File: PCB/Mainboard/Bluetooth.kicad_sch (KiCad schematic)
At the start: 22 parts, among them J10 U.FL, J11 JST-PH 01x02, U10 BTM331

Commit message: Update schematic and lay-out
- Swap out CP2102N, ATmega328PB and CP with new Kicad 6 symbol
- Correct all links to point to new zoudio_symbols and zoudio_footprint libraries
- Lay-out updated, only antenna is left to update.
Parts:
- AE1: footprint ZOUDIO-footprints:Texas_SWRA117D_2.4GHz_Left -> zoudio_footprints:Texas_SWRA117D_2.4GHz_Left
- U10: footprint ZOUDIO-footprints:BTM331 -> zoudio_footprints:BTM331; symbol ZOUDIO-symbols:BTM331 -> zoudio_symbols:BTM331
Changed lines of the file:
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@@
     (pin "2")
   )
-  (symbol (lib_id "ZOUDIO-symbols:BTM331") (at 114.3 101.6 0) (unit 1)
+  (symbol (lib_id "zoudio_symbols:BTM331") (at 114.3 101.6 0) (unit 1)
     (in_bom yes) (on_board yes)
     (property "Reference" "U10" (id 0) (at 114.3 100.33 0))
     (property "Value" "BTM331" (id 1) (at 114.3 102.87 0))
-    (property "Footprint" "ZOUDIO-footprints:BTM331" (id 2) (at 102.87 93.98 0)
+    (property "Footprint" "zoudio_footprints:BTM331" (id 2) (at 102.87 93.98 0)
       (effects (font (size 1.27 1.27)) hide)
     )
@@
       (effects (font (size 1.27 1.27)) (justify right))
     )
-    (property "Footprint" "ZOUDIO-footprints:Texas_SWRA117D_2.4GHz_Left" (id 2) (at 123.19 52.07 0)
-      (effects (font (size 1.27 1.27)) hide)
-    )
+    (property "Footprint" "zoudio_footprints:Texas_SWRA117D_2.4GHz_Left" (id 2) (at 123.19 52.07 0)
+      (effects (font (size 1.27 1.27)) hide)
+    )

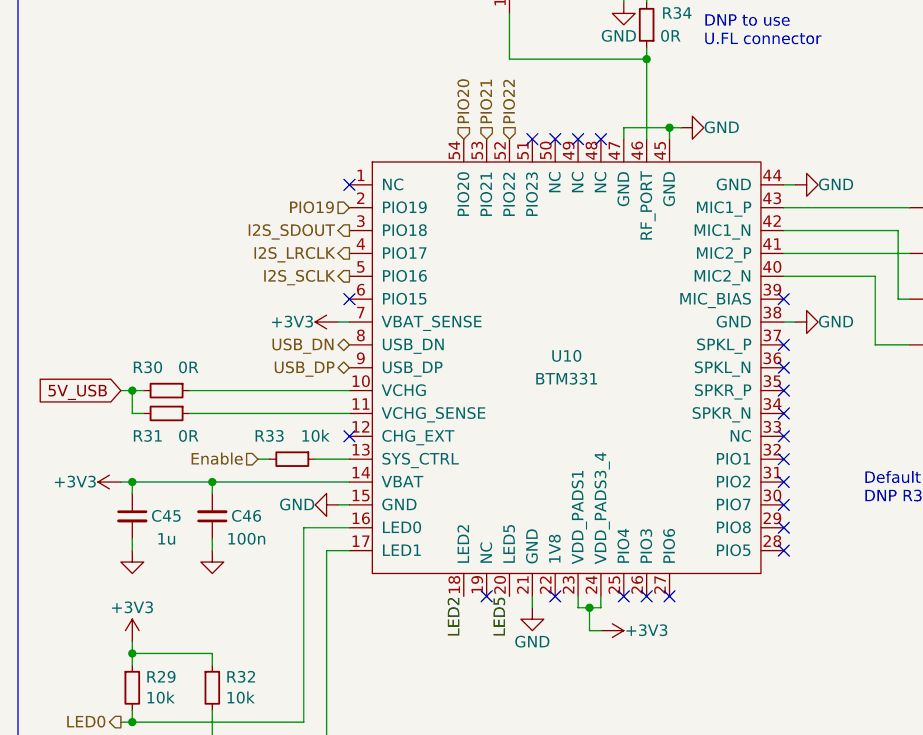
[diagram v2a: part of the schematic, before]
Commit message: Mainboard: version 1.1.1
- No change in electrical connectivity
- Make 3D model more complete
- Improvements in paste layer for manufacturability
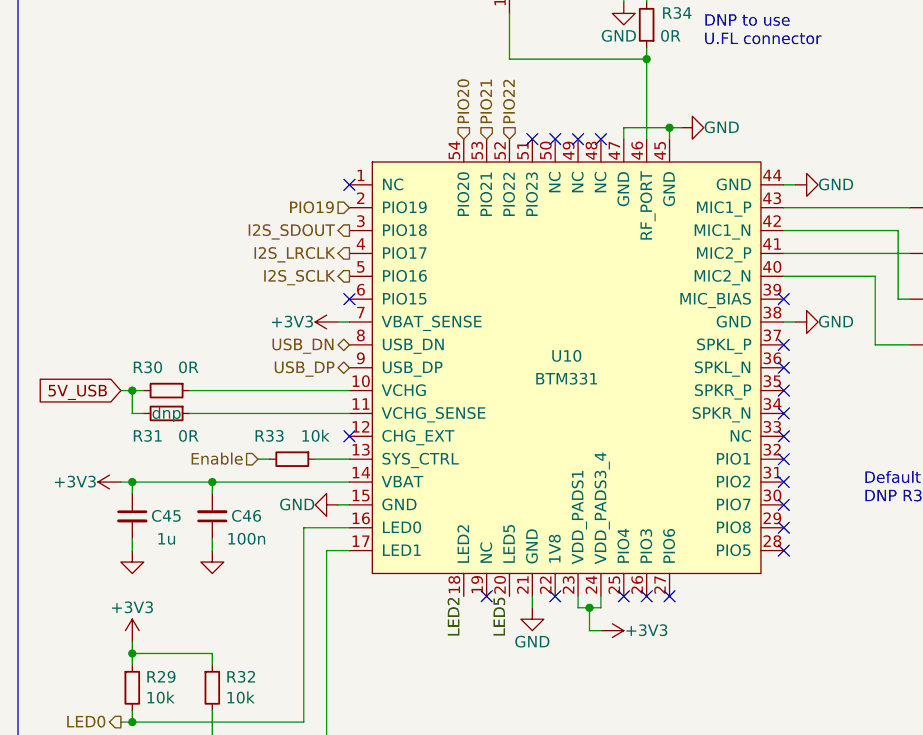
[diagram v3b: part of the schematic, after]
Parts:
- R31: Config (none) -> dnp
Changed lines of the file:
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@@
   (title_block
     (title "4x38W amp with DSP and BT")
-    (date "2022-02-12")
-    (rev "1.1")
+    (date "2022-04-17")
+    (rev "1.1.1")
     (company "ZOUDIO")
   )
@@
       (effects (font (size 1.27 1.27)) hide)
     )
-    (pin "1")
-    (pin "2")
+    (property "Config" "dnp" (id 6) (at 69.85 106.68 90))
+    (pin "1")
+    (pin "2")
